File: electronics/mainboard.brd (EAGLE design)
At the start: 158.8 x 159.4 mm, 96 parts, among them T1 NPN_BC817,215, T2 NPN_BC817,215, T3 NPN_BC817,215, U1 CD4051BM, X1 JST-XH-10-PIN-LONG-PAD, X2 JST-XH-10-PIN-LONG-PAD, X3 JST-XH-10-PIN-LONG-PAD, X4 JST-XH-10-PIN-LONG-PAD, X5 JST-XH-10-PIN-LONG-PAD

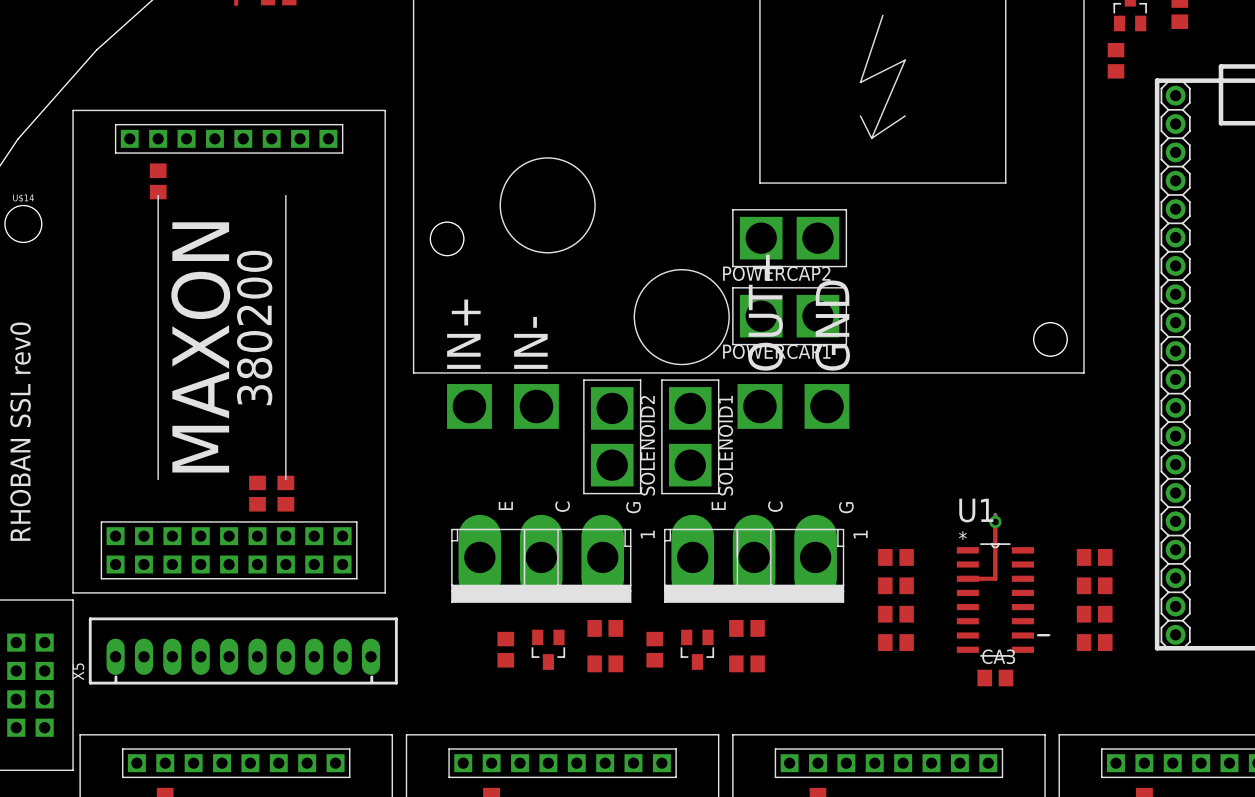
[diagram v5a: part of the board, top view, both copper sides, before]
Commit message: Adding PWM compatibility pins
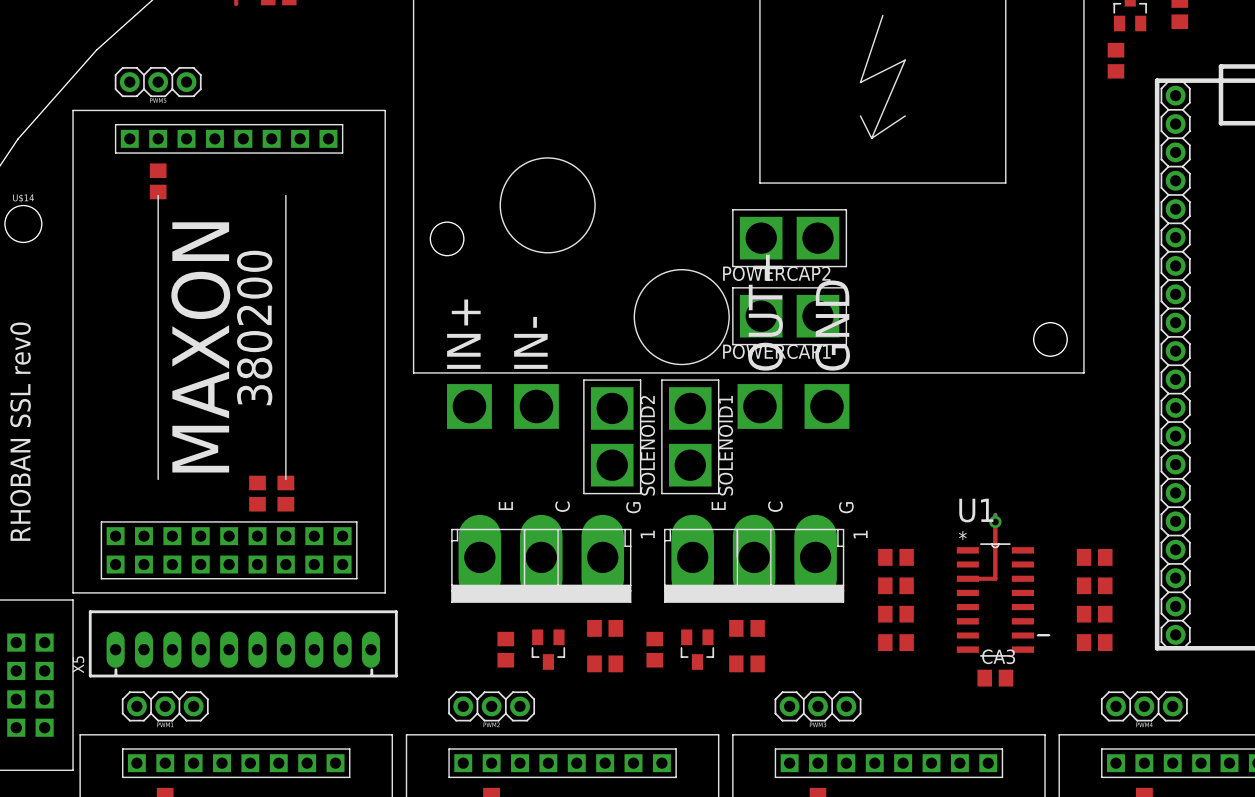
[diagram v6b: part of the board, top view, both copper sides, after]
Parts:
- added PWM1, PWM2, PWM3, PWM4, PWM5: CONNEC_1X03, rhoban:CONNEC_1X03
- moved X5 0.63 mm to (-40.0, 5.71)
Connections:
- net GND: now also PWM1.1, PWM2.1, PWM3.1, PWM4.1, PWM5.1
- net M1_SPEED: now also PWM1.3
- net M2_SPEED: now also PWM2.3
- net M3_SPEED: now also PWM3.3
- net M4_SPEED: now also PWM4.3
- net M5_SPEED: now also PWM5.3
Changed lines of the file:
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@@
 <setting verticaltext="up"/>
 </settings>
-<grid distance="0.1" unitdist="mm" unit="mm" style="lines" multiple="1" display="no" altdistance="0.025" altunitdist="inch" altunit="inch"/>
+<grid distance="0.025" unitdist="inch" unit="inch" style="lines" multiple="1" display="no" altdistance="0.025" altunitdist="inch" altunit="inch"/>
 <layers>
 <layer number="1" name="Top" color="4" fill="1" visible="yes" active="yes"/>
@@
 <element name="X3" library="Rembrandt Electronics - JST XH Connectors v1-0" package="JST-XH-10-PACKAGE-LONG-PAD" value="JST-XH-10-PIN-LONG-PAD" x="17.78" y="-49.53"/>
 <element name="X4" library="Rembrandt Electronics - JST XH Connectors v1-0" package="JST-XH-10-PACKAGE-LONG-PAD" value="JST-XH-10-PIN-LONG-PAD" x="46.99" y="-49.53"/>
-<element name="X5" library="Rembrandt Electronics - JST XH Connectors v1-0" package="JST-XH-10-PACKAGE-LONG-PAD" value="JST-XH-10-PIN-LONG-PAD" x="-40.005" y="5.08"/>
+<element name="X5" library="Rembrandt Electronics - JST XH Connectors v1-0" package="JST-XH-10-PACKAGE-LONG-PAD" value="JST-XH-10-PIN-LONG-PAD" x="-40.005" y="5.715"/>
 <element name="COM2" library="rhoban" package="NRF24L01" value="NRF24L01" x="64.135" y="6.985" rot="R270"/>
 <element name="COM3" library="rhoban" package="NRF24L01" value="NRF24L01" x="6.985" y="-58.42" rot="R180"/>
@@
 </element>
 <element name="XT1" library="rhoban" package="XT60" value="CONNEC_ALIM" x="-57.785" y="-27.94" rot="R90"/>
+<element name="PWM1" library="rhoban" package="CONNEC_1X03" value="CONNEC_1X03" x="-45.72" y="1.905" rot="R180"/>
+<element name="PWM2" library="rhoban" package="CONNEC_1X03" value="CONNEC_1X03" x="-16.51" y="1.905" rot="R180"/>
+<element name="PWM3" library="rhoban" package="CONNEC_1X03" value="CONNEC_1X03" x="12.7" y="1.905" rot="R180"/>
+<element name="PWM4" library="rhoban" package="CONNEC_1X03" value="CONNEC_1X03" x="41.91" y="1.905" rot="R180"/>
+<element name="PWM5" library="rhoban" package="CONNEC_1X03" value="CONNEC_1X03" x="-46.355" y="57.785" rot="R180"/>
 </elements>
 <signals>
@@
 <contactref element="CA7" pad="2"/>
 <contactref element="XT1" pad="GND"/>
-<wire x1="-44.45" y1="-49.53" x2="-61.785" y2="-16.44" width="0" layer="19" extent="1-1"/>
+<contactref element="PWM1" pad="1"/>
+<contactref element="PWM2" pad="1"/>
+<contactref element="PWM3" pad="1"/>
+<contactref element="PWM4" pad="1"/>
+<contactref element="PWM5" pad="1"/>
+<wire x1="43.18" y1="0.635" x2="-45.085" y2="56.515" width="0" layer="19" extent="1-1"/>
+<wire x1="13.97" y1="0.635" x2="43.18" y2="0.635" width="0" layer="19" extent="1-1"/>
+<wire x1="-15.24" y1="0.635" x2="13.97" y2="0.635" width="0" layer="19" extent="1-1"/>
+<wire x1="-44.45" y1="0.635" x2="-15.24" y2="0.635" width="0" layer="19" extent="1-1"/>
+<wire x1="-44.45" y1="-49.53" x2="-44.45" y2="0.635" width="0" layer="19" extent="1-1"/>
 <wire x1="-40.64" y1="-42.545" x2="-44.45" y2="-49.53" width="0" layer="19" extent="1-1"/>
 <wire x1="-40.64" y1="-40.005" x2="-40.64" y2="-42.545" width="0" layer="19" extent="1-1"/>
@@
 <wire x1="-46.99" y1="-9.205" x2="-41.275" y2="-21.27" width="0" layer="19" extent="1-1"/>
 <wire x1="-44.45" y1="-4.445" x2="-46.99" y2="-9.205" width="0" layer="19" extent="1-1"/>
-<wire x1="-43.815" y1="5.08" x2="-44.45" y2="-4.445" width="0" layer="19" extent="1-1"/>
-<wire x1="-41.275" y1="13.335" x2="-43.815" y2="5.08" width="0" layer="19" extent="1-1"/>
+<wire x1="-43.815" y1="5.715" x2="-44.45" y2="-4.445" width="0" layer="19" extent="1-1"/>
+<wire x1="-41.275" y1="13.335" x2="-43.815" y2="5.715" width="0" layer="19" extent="1-1"/>
 <wire x1="-41.275" y1="15.875" x2="-41.275" y2="13.335" width="0" layer="19" extent="1-1"/>
 <wire x1="-36.195" y1="15.875" x2="-41.275" y2="15.875" width="0" layer="19" extent="1-1"/>
@@
 <wire x1="43.18" y1="-4.445" x2="40.64" y2="-9.205" width="0" layer="19" extent="1-1"/>
 <wire x1="-13.765" y1="27.48" x2="-18.835" y2="13.97" width="0" layer="19" extent="1-1"/>
+<wire x1="-61.785" y1="-16.44" x2="-48.895" y2="-23.3934" width="0" layer="19" extent="1-1"/>
 <wire x1="24.8412" y1="5.715" x2="13.97" y2="-4.445" width="0" layer="19" extent="1-1"/>
 <wire x1="24.8412" y1="6.985" x2="24.8412" y2="5.715" width="0" layer="19" extent="1-1"/>
@@
 <wire x1="49.53" y1="-42.545" x2="49.53" y2="-37.145" width="0" layer="19" extent="1-1"/>
 <wire x1="45.72" y1="-49.53" x2="49.53" y2="-42.545" width="0" layer="19" extent="1-1"/>
-<wire x1="-41.275" y1="5.08" x2="-51.435" y2="-17.2466" width="0" layer="19" extent="1-1"/>
-<wire x1="-38.735" y1="13.335" x2="-41.275" y2="5.08" width="0" layer="19" extent="1-1"/>
+<wire x1="-41.275" y1="5.715" x2="-51.435" y2="-17.2466" width="0" layer="19" extent="1-1"/>
+<wire x1="-38.735" y1="13.335" x2="-41.275" y2="5.715" width="0" layer="19" extent="1-1"/>
 <wire x1="-38.735" y1="18.735" x2="-38.735" y2="13.335" width="0" layer="19" extent="1-1"/>
 </signal>
@@
 <contactref element="U$6" pad="26"/>
 <contactref element="MAPLE" pad="X3"/>
-<wire x1="-49.53" y1="-4.445" x2="58.68" y2="17.2" width="0" layer="19" extent="1-1"/>
+<contactref element="PWM1" pad="3"/>
+<wire x1="-49.53" y1="-4.445" x2="-49.53" y2="0.635" width="0" layer="19" extent="1-1"/>
+<wire x1="58.68" y1="17.2" x2="-49.53" y2="-4.445" width="0" layer="19" extent="1-1"/>
 </signal>
 <signal name="N$16">
@@
 <contactref element="U$7" pad="26"/>
 <contactref element="MAPLE" pad="X4"/>
-<wire x1="-20.32" y1="-4.445" x2="58.68" y2="19.74" width="0" layer="19" extent="1-1"/>
+<contactref element="PWM2" pad="3"/>
+<wire x1="-20.32" y1="-4.445" x2="-20.32" y2="0.635" width="0" layer="19" extent="1-1"/>
+<wire x1="58.68" y1="19.74" x2="-20.32" y2="-4.445" width="0" layer="19" extent="1-1"/>
 </signal>
 <signal name="M2_HALL3">
@@
 <contactref element="U$8" pad="26"/>
 <contactref element="MAPLE" pad="X5"/>
-<wire x1="8.89" y1="-4.445" x2="58.68" y2="22.28" width="0" layer="19" extent="1-1"/>
+<contactref element="PWM3" pad="3"/>
+<wire x1="8.89" y1="-4.445" x2="8.89" y2="0.635" width="0" layer="19" extent="1-1"/>
+<wire x1="58.68" y1="22.28" x2="8.89" y2="-4.445" width="0" layer="19" extent="1-1"/>
 </signal>
 <signal name="M3_DIR">
@@
 <contactref element="U$9" pad="26"/>
 <contactref element="MAPLE" pad="X8"/>
-<wire x1="38.1" y1="-4.445" x2="58.68" y2="29.9" width="0" layer="19" extent="1-1"/>
+<contactref element="PWM4" pad="3"/>
+<wire x1="38.1" y1="-4.445" x2="38.1" y2="0.635" width="0" layer="19" extent="1-1"/>
+<wire x1="58.68" y1="29.9" x2="38.1" y2="-4.445" width="0" layer="19" extent="1-1"/>
 </signal>
 <signal name="N$32">
@@
 <contactref element="U$10" pad="15"/>
 <contactref element="X5" pad="7"/>
-<wire x1="-33.655" y1="13.335" x2="-36.195" y2="5.08" width="0" layer="19" extent="1-1"/>
+<wire x1="-33.655" y1="13.335" x2="-36.195" y2="5.715" width="0" layer="19" extent="1-1"/>
 </signal>
 <signal name="M5_HALL1">
 <contactref element="U$10" pad="13"/>
 <contactref element="X5" pad="6"/>
-<wire x1="-36.195" y1="13.335" x2="-38.735" y2="5.08" width="0" layer="19" extent="1-1"/>
+<wire x1="-36.195" y1="13.335" x2="-38.735" y2="5.715" width="0" layer="19" extent="1-1"/>
 </signal>
 <signal name="M5_W3" class="2">
@@
 <contactref element="U$10" pad="5"/>
 <contactref element="X5" pad="3"/>
-<wire x1="-46.355" y1="13.335" x2="-46.355" y2="5.08" width="0" layer="19" extent="1-1"/>
+<wire x1="-46.355" y1="13.335" x2="-46.355" y2="5.715" width="0" layer="19" extent="1-1"/>
 <wire x1="-46.355" y1="15.875" x2="-46.355" y2="13.335" width="0" layer="19" extent="1-1"/>
 </signal>
@@
 <contactref element="U$10" pad="3"/>
 <contactref element="X5" pad="2"/>
-<wire x1="-48.895" y1="13.335" x2="-48.895" y2="5.08" width="0" layer="19" extent="1-1"/>
+<wire x1="-48.895" y1="13.335" x2="-48.895" y2="5.715" width="0" layer="19" extent="1-1"/>
 <wire x1="-48.895" y1="15.875" x2="-48.895" y2="13.335" width="0" layer="19" extent="1-1"/>
 </signal>
@@
 <contactref element="U$10" pad="1"/>
 <contactref element="X5" pad="1"/>
-<wire x1="-51.435" y1="13.335" x2="-51.435" y2="5.08" width="0" layer="19" extent="1-1"/>
+<wire x1="-51.435" y1="13.335" x2="-51.435" y2="5.715" width="0" layer="19" extent="1-1"/>
 <wire x1="-51.435" y1="15.875" x2="-51.435" y2="13.335" width="0" layer="19" extent="1-1"/>
 </signal>
@@
 <contactref element="U$10" pad="26"/>
 <contactref element="MAPLE" pad="X9"/>
-<wire x1="-50.165" y1="51.435" x2="58.68" y2="32.44" width="0" layer="19" extent="1-1"/>
+<contactref element="PWM5" pad="3"/>
+<wire x1="-50.165" y1="51.435" x2="-50.165" y2="56.515" width="0" layer="19" extent="1-1"/>
+<wire x1="58.68" y1="32.44" x2="-50.165" y2="51.435" width="0" layer="19" extent="1-1"/>
 </signal>
 <signal name="MT_HALL3">

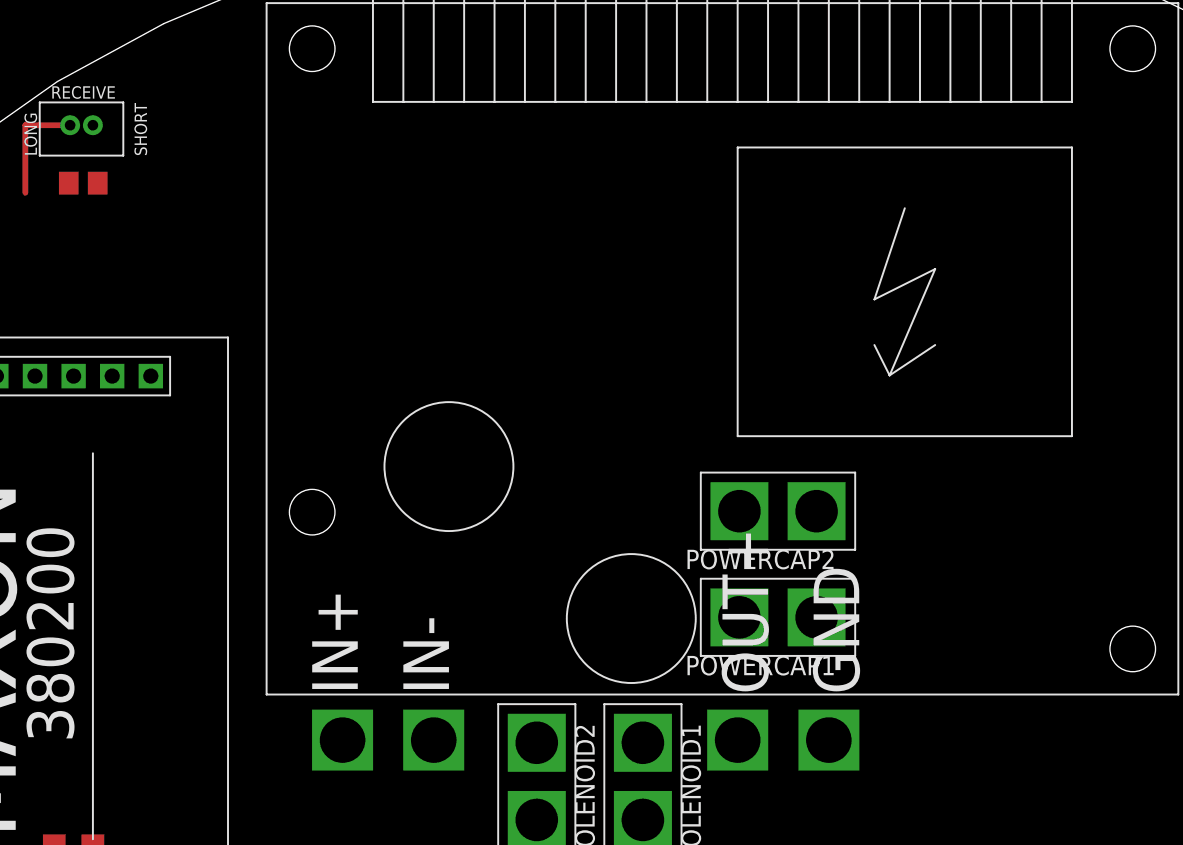
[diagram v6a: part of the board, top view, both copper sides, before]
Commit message: Adding boost_en and cap to control charge
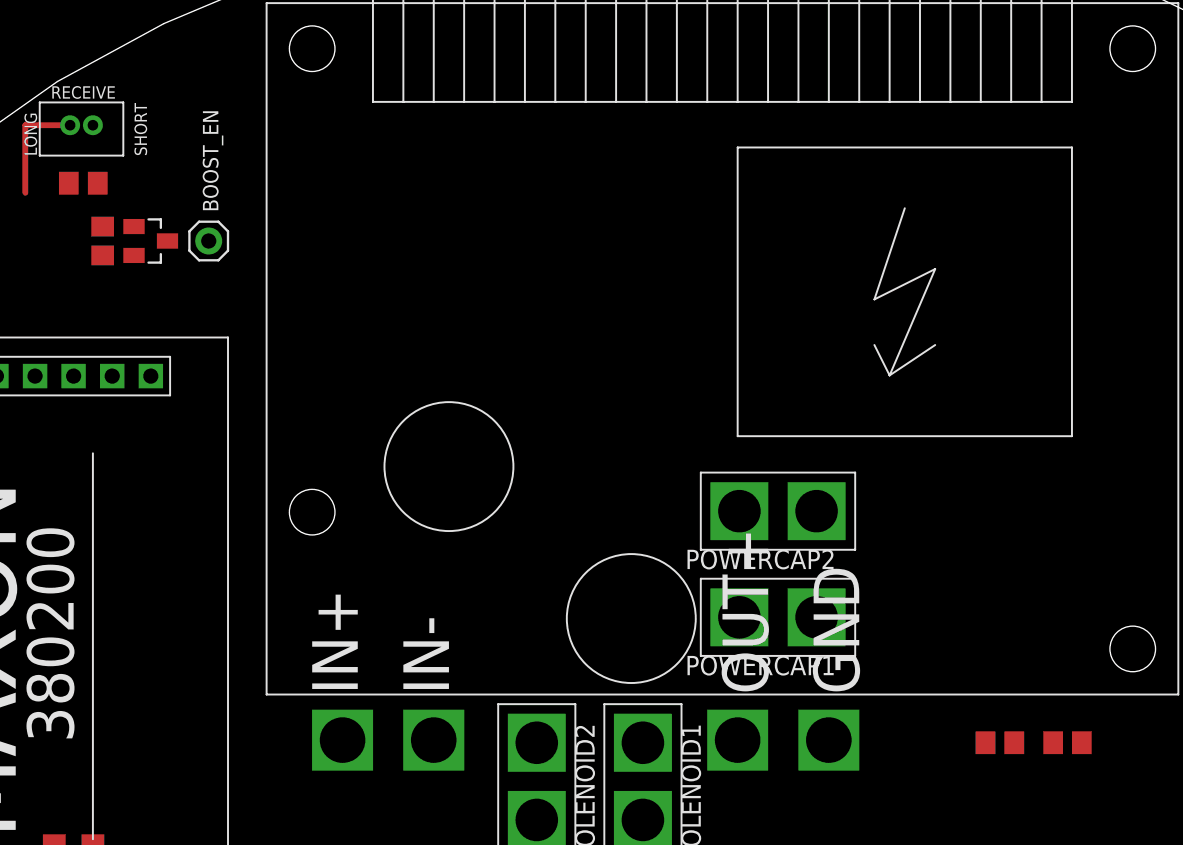
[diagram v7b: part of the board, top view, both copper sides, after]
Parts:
- added BOOST_EN: CONNEC_1X01, rhoban:CONNEC_1X01
- added R34: 2M, rhoban:R0805
- added R35: 10K, rhoban:R0805
- added R36: 3K, rhoban:R0805
- added U$15: NPN_BC817,215, rhoban:SOT-23
- R8: value 2K -> 3K
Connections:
- new net BOOST_EN: MAPLE.X27, R36.2
- new net CAP: MAPLE.X6, R34.1, R35.2
- new net N$37: BOOST_EN.1, U$15.3
- new net N$38: R36.1, U$15.1
- net GND: now also R35.1, U$15.2
- net KICK1: now also MAPLE.X0; no longer MAPLE.X7
- net KICK2: now also MAPLE.X1; no longer MAPLE.X6
- net VBOOST: now also R34.2
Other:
- board text added: "BOOST_EN"
